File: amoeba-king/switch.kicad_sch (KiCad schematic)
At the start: 2 parts

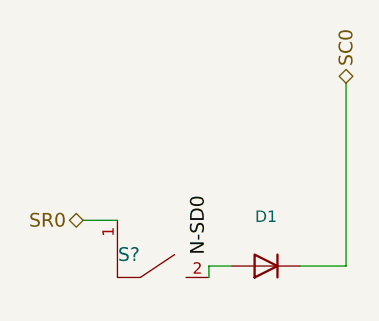
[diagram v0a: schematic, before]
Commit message: Added row via to be used as an anchor point for cabling.
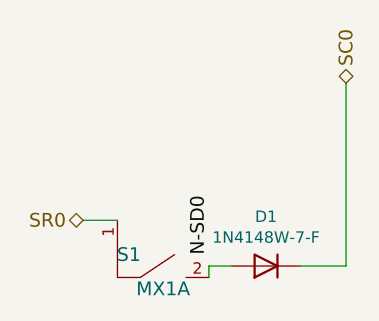
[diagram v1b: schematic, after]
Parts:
- D1: value (none) -> 1N4148W-7-F; footprint (none) -> Diode_SMD:D_SOD-123
- S1: renamed from S?; value (none) -> MX1A; footprint (none) -> amoeba-modules:Kailh_MX_Socket
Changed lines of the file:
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@@
   (symbol (lib_id "amoeba-king-rescue:MX1A-amoeba-rescue-amoeba-royale-rescue") (at 121.92 95.25 0) (unit 1)
     (in_bom yes) (on_board yes)
-    (property "Reference" "S?" (id 0) (at 118.11 88.9 0)
+    (property "Reference" "S1" (id 0) (at 118.11 88.9 0)
       (effects (font (size 1.524 1.524)))
     )
-    (property "Value" "" (id 1) (at 121.92 92.71 0)
+    (property "Value" "MX1A" (id 1) (at 121.92 92.71 0)
       (effects (font (size 1.524 1.524)))
     )
-    (property "Footprint" "" (id 2) (at 121.92 95.25 0)
+    (property "Footprint" "amoeba-modules:Kailh_MX_Socket" (id 2) (at 121.92 95.25 0)
       (effects (font (size 1.524 1.524)) hide)
     )
@@
     (in_bom yes) (on_board yes)
     (property "Reference" "D1" (id 0) (at 133.35 84.6836 0))
-    (property "Value" "" (id 1) (at 133.35 86.995 0))
-    (property "Footprint" "" (id 2) (at 133.35 90.17 0)
+    (property "Value" "1N4148W-7-F" (id 1) (at 133.35 86.995 0))
+    (property "Footprint" "Diode_SMD:D_SOD-123" (id 2) (at 133.35 90.17 0)
       (effects (font (size 1.27 1.27)) hide)
     )
